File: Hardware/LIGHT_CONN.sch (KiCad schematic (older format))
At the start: 73 parts, among them P10 AI_RGB, P11 AI_RGB, P12 AI_RGB, P13 AI_RGB, P14 CONN_01X04, P15 AI_RGB, P16 AI_RGB, P17 AI_RGB, P18 AI_RGB, P19 AI_RGB, P2 AI_RGB, P20 CONN_01X04, P21 AI_RGB, P3 CONN_01X04, P4 AI_RGB, P5 AI_RGB, P6 AI_RGB, P7 AI_RGB, P8 AI_RGB, P9 CONN_01X04, Q10 MOSFET_N, Q11 MOSFET_N, Q12 MOSFET_N, Q13 MOSFET_N, Q2 MOSFET_N, Q3 MOSFET_N, Q4 MOSFET_N, Q5 MOSFET_N, Q6 MOSFET_N, Q7 MOSFET_N, Q8 MOSFET_N, Q9 MOSFET_N, U10 PCA9685BS

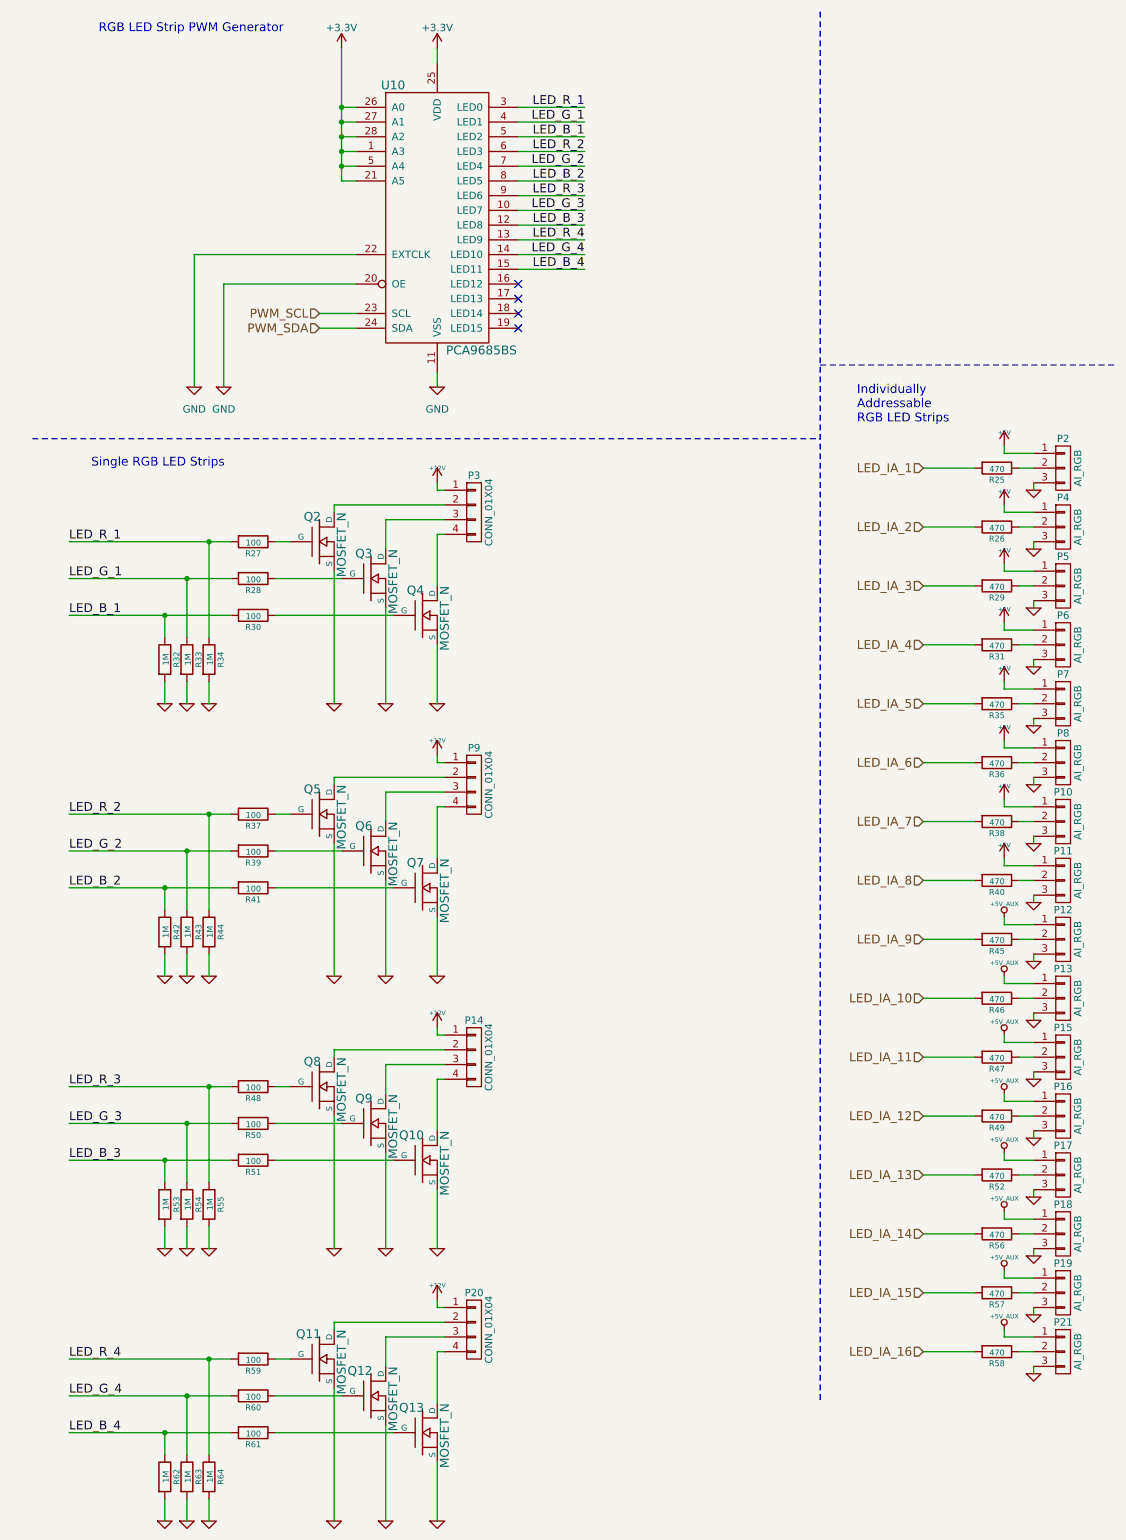
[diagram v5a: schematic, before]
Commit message: Finished converting to global labels
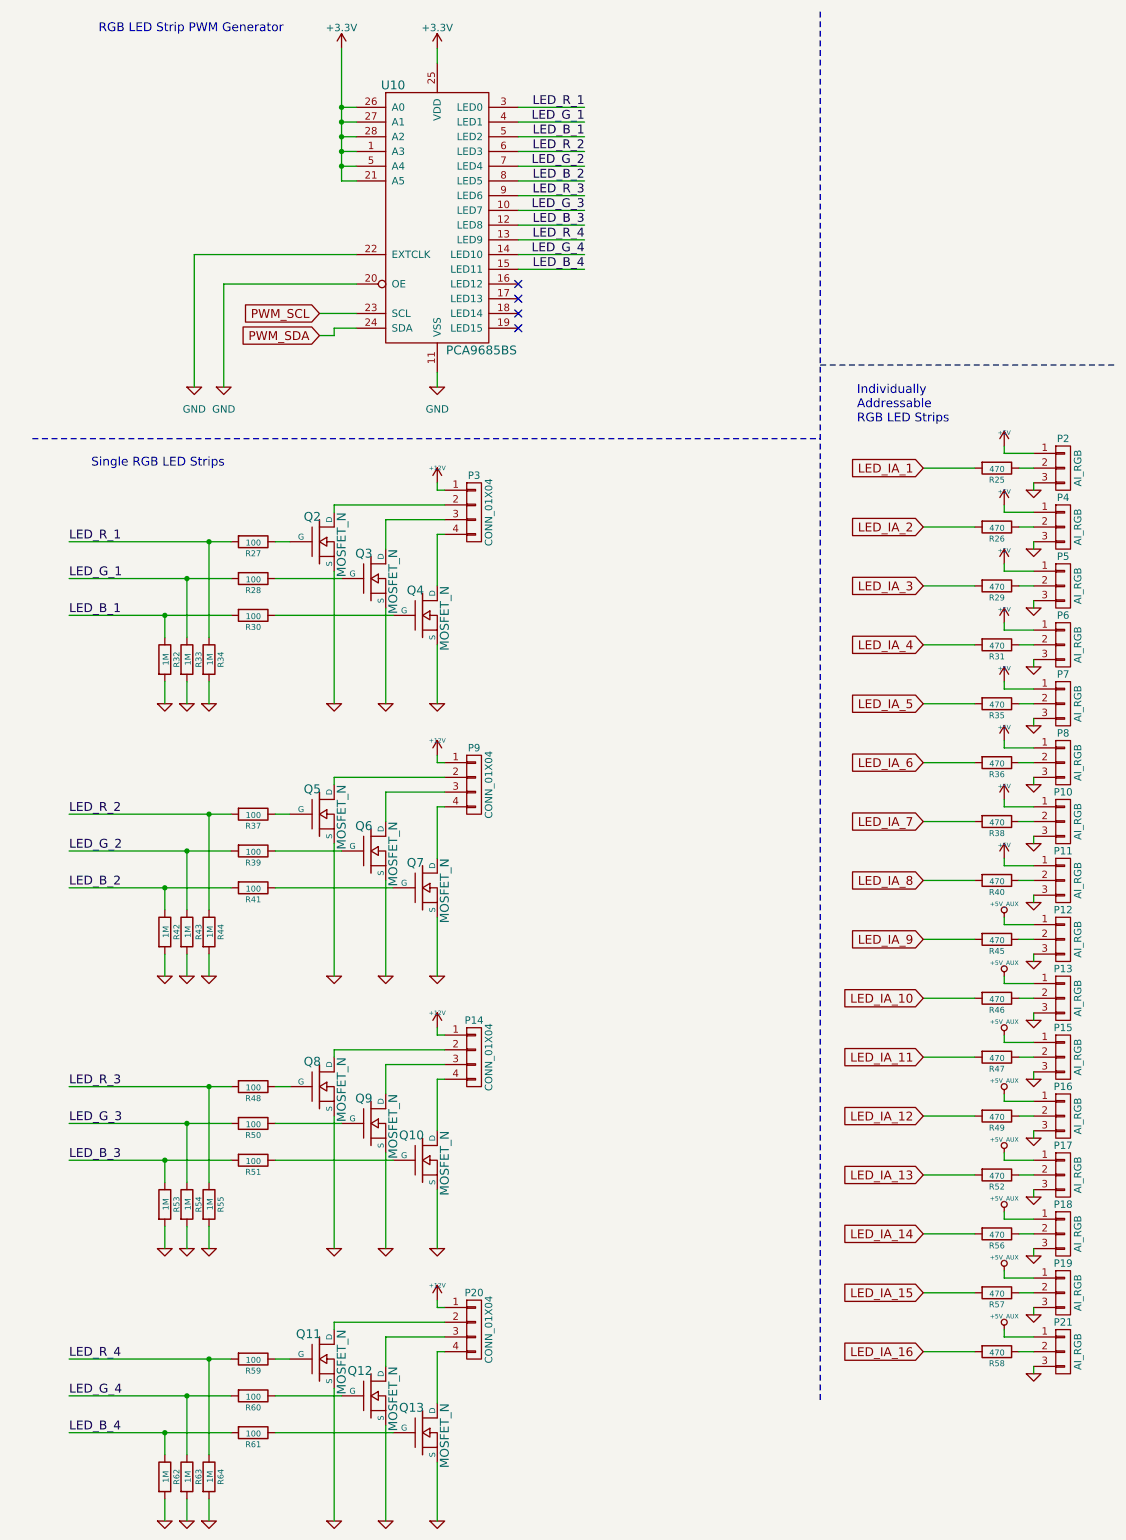
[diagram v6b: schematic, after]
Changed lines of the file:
@@
 $Descr A4 8268 11693 portrait
 encoding utf-8
-Sheet 5 8
+Sheet 10 10
 Title ""
 Date ""
@@
 	1    0    0    -1
 $EndComp
-Text HLabel 6500 3600 0    60   Input ~ 0
-LED_IA_1
-Text HLabel 6500 4000 0    60   Input ~ 0
-LED_IA_2
-Text HLabel 6500 4400 0    60   Input ~ 0
-LED_IA_3
-Text HLabel 6500 4800 0    60   Input ~ 0
-LED_IA_4
-Text HLabel 6500 5200 0    60   Input ~ 0
-LED_IA_5
-Text HLabel 6500 5600 0    60   Input ~ 0
-LED_IA_6
-Text HLabel 6500 6000 0    60   Input ~ 0
-LED_IA_7
-Text HLabel 6500 6400 0    60   Input ~ 0
-LED_IA_8
-Text HLabel 6500 6800 0    60   Input ~ 0
-LED_IA_9
-Text HLabel 6500 7200 0    60   Input ~ 0
-LED_IA_10
-Text HLabel 6500 7600 0    60   Input ~ 0
-LED_IA_11
-Text HLabel 6500 8000 0    60   Input ~ 0
-LED_IA_12
-Text HLabel 6500 8400 0    60   Input ~ 0
-LED_IA_13
-Text HLabel 6500 8800 0    60   Input ~ 0
-LED_IA_14
-Text HLabel 6500 9200 0    60   Input ~ 0
-LED_IA_15
-Text HLabel 6500 9600 0    60   Input ~ 0
-LED_IA_16
 $Comp
 L PCA9685BS U10
@@
 NoConn ~ 3750 2550
 NoConn ~ 3750 2650
-Text HLabel 2400 2550 0    60   Input ~ 0
-PWM_SCL
-Text HLabel 2400 2650 0    60   Input ~ 0
-PWM_SDA
 $Comp
 L GND-RESCUE-museV2 #PWR67
@@
 	1550 2150 2650 2150
 Wire Wire Line
-	2400 2650 2650 2650
-Wire Wire Line
 	2400 2550 2650 2550
 Wire Wire Line
@@
 Wire Notes Line
 	450  3400 5800 3400
-Wire Notes Line
-	5800 500  5800 9950
 Wire Wire Line
 	2500 9400 3250 9400
@@
 Wire Wire Line
 	7250 9600 7150 9600
+Text GLabel 2400 2550 0    60   Input ~ 0
+PWM_SCL
+Text GLabel 2400 2700 0    60   Input ~ 0
+PWM_SDA
+Wire Wire Line
+	2400 2700 2500 2700
+Wire Wire Line
+	2500 2700 2500 2650
+Wire Wire Line
+	2500 2650 2650 2650
+Text GLabel 6500 3600 0    60   Input ~ 0
+LED_IA_1
+Wire Notes Line
+	5800 500  5800 9950
+Text GLabel 6500 4000 0    60   Input ~ 0
+LED_IA_2
+Text GLabel 6500 4400 0    60   Input ~ 0
+LED_IA_3
+Text GLabel 6500 4800 0    60   Input ~ 0
+LED_IA_4
+Text GLabel 6500 5200 0    60   Input ~ 0
+LED_IA_5
+Text GLabel 6500 5600 0    60   Input ~ 0
+LED_IA_6
+Text GLabel 6500 6000 0    60   Input ~ 0
+LED_IA_7
+Text GLabel 6500 6400 0    60   Input ~ 0
+LED_IA_8
+Text GLabel 6500 6800 0    60   Input ~ 0
+LED_IA_9
+Text GLabel 6500 7200 0    60   Input ~ 0
+LED_IA_10
+Text GLabel 6500 7600 0    60   Input ~ 0
+LED_IA_11
+Text GLabel 6500 8000 0    60   Input ~ 0
+LED_IA_12
+Text GLabel 6500 8400 0    60   Input ~ 0
+LED_IA_13
+Text GLabel 6500 8800 0    60   Input ~ 0
+LED_IA_14
+Text GLabel 6500 9200 0    60   Input ~ 0
+LED_IA_15
+Text GLabel 6500 9600 0    60   Input ~ 0
+LED_IA_16
 $EndSCHEMATC

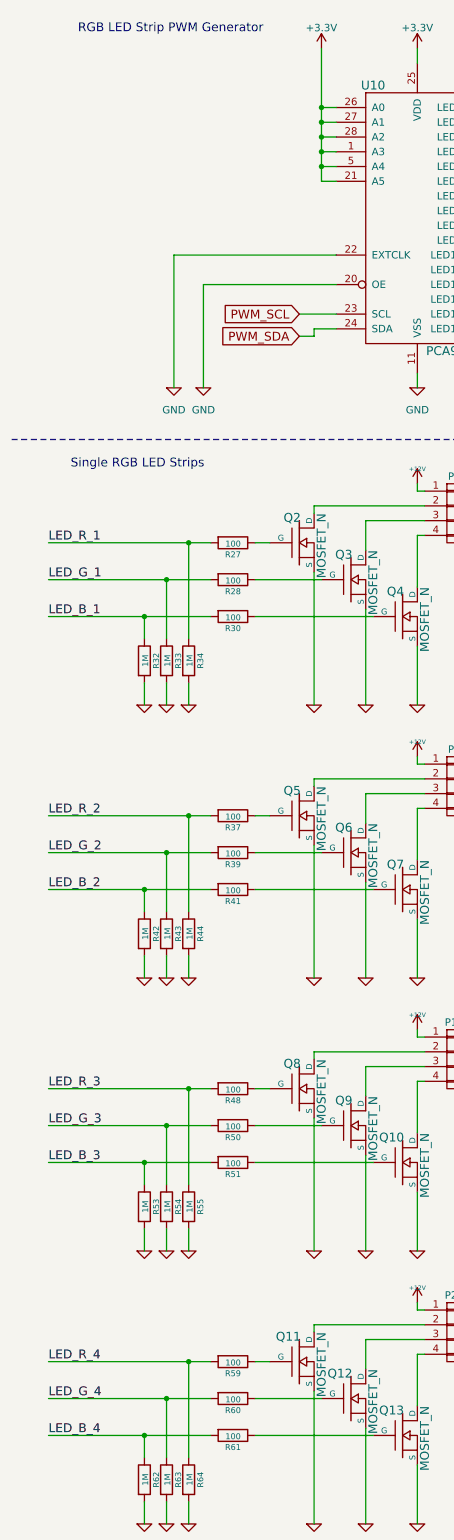
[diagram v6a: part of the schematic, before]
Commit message: Updated I2C pullup resistors and labels
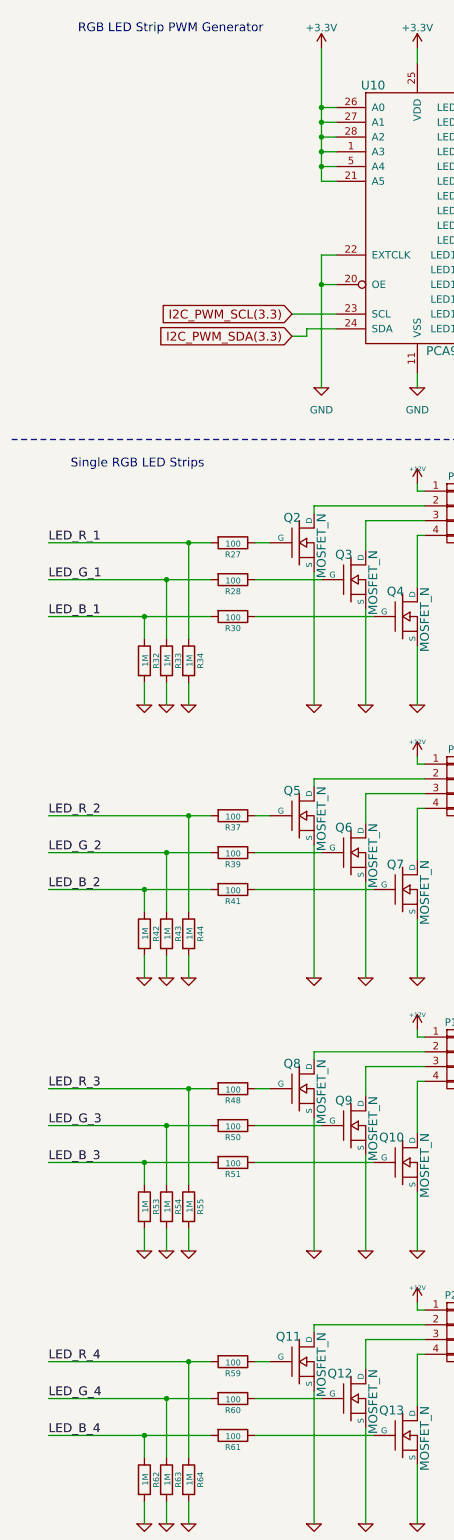
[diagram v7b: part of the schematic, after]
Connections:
- net PWM_SCL renamed I2C_PWM_SCL(3.3)
- net PWM_SDA renamed I2C_PWM_SDA(3.3)
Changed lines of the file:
@@
 NoConn ~ 3750 2550
 NoConn ~ 3750 2650
-$Comp
-L GND-RESCUE-museV2 #PWR67
-U 1 1 57E689F1
-P 1550 3050
-F 0 "#PWR67" H 1550 2800 50  0001 C CNN
-F 1 "GND" H 1550 2900 50  0000 C CNN
-F 2 "" H 1550 3050 50  0000 C CNN
-F 3 "" H 1550 3050 50  0000 C CNN
-	1    1550 3050
-	1    0    0    -1
-$EndComp
-Wire Wire Line
-	1550 3050 1550 2150
-Wire Wire Line
-	1550 2150 2650 2150
-Wire Wire Line
-	2400 2550 2650 2550
+Wire Wire Line
+	2350 2550 2650 2550
 Wire Wire Line
 	3750 2250 4200 2250
@@
 	6500 9600 6850 9600
 Wire Wire Line
-	700  4600 1800 4600
-Wire Wire Line
-	700  4350 1800 4350
-Wire Wire Line
-	700  4100 1800 4100
+	700  4600 1350 4600
+Wire Wire Line
+	1350 4600 1800 4600
+Wire Wire Line
+	700  4350 1500 4350
+Wire Wire Line
+	1500 4350 1800 4350
+Wire Wire Line
+	700  4100 1650 4100
+Wire Wire Line
+	1650 4100 1800 4100
 Wire Wire Line
 	2100 4350 2550 4350
@@
 	3200 7050 3200 6650
 Wire Wire Line
-	700  6450 1800 6450
-Wire Wire Line
-	700  6200 1800 6200
-Wire Wire Line
-	700  5950 1800 5950
+	700  6450 1350 6450
+Wire Wire Line
+	1350 6450 1800 6450
+Wire Wire Line
+	700  6200 1500 6200
+Wire Wire Line
+	1500 6200 1800 6200
+Wire Wire Line
+	700  5950 1650 5950
+Wire Wire Line
+	1650 5950 1800 5950
 Wire Wire Line
 	2100 6200 2550 6200
@@
 	3200 8900 3200 8500
 Wire Wire Line
-	700  8300 1800 8300
-Wire Wire Line
-	700  8050 1800 8050
-Wire Wire Line
-	700  7800 1800 7800
+	700  8300 1350 8300
+Wire Wire Line
+	1350 8300 1800 8300
+Wire Wire Line
+	700  8050 1500 8050
+Wire Wire Line
+	1500 8050 1800 8050
+Wire Wire Line
+	700  7800 1650 7800
+Wire Wire Line
+	1650 7800 1800 7800
 Wire Wire Line
 	2100 8050 2550 8050
@@
 	3200 10750 3200 10350
 Wire Wire Line
-	700  10150 1800 10150
-Wire Wire Line
-	700  9900 1800 9900
-Wire Wire Line
-	700  9650 1800 9650
+	700  10150 1350 10150
+Wire Wire Line
+	1350 10150 1800 10150
+Wire Wire Line
+	700  9900 1500 9900
+Wire Wire Line
+	1500 9900 1800 9900
+Wire Wire Line
+	700  9650 1650 9650
+Wire Wire Line
+	1650 9650 1800 9650
 Wire Wire Line
 	2100 9900 2550 9900
@@
 $EndComp
 Wire Wire Line
-	2550 750  2550 1650
+	2550 750  2550 1150
+Wire Wire Line
+	2550 1150 2550 1250
+Wire Wire Line
+	2550 1250 2550 1350
+Wire Wire Line
+	2550 1350 2550 1450
+Wire Wire Line
+	2550 1450 2550 1550
+Wire Wire Line
+	2550 1550 2550 1650
 Wire Wire Line
 	2550 1650 2650 1650
@@
 L GND-RESCUE-museV2 #PWR68
 U 1 1 57EF1660
-P 1750 3050
-F 0 "#PWR68" H 1750 2800 50  0001 C CNN
-F 1 "GND" H 1750 2900 50  0000 C CNN
-F 2 "" H 1750 3050 50  0000 C CNN
-F 3 "" H 1750 3050 50  0000 C CNN
-	1    1750 3050
+P 2550 3050
+F 0 "#PWR68" H 2550 2800 50  0001 C CNN
+F 1 "GND" H 2550 2900 50  0000 C CNN
+F 2 "" H 2550 3050 50  0000 C CNN
+F 3 "" H 2550 3050 50  0000 C CNN
+	1    2550 3050
 	1    0    0    -1
 $EndComp
 Wire Wire Line
-	1750 2350 1750 3050
-Wire Wire Line
-	1750 2350 2650 2350
+	2550 2150 2550 2350
+Wire Wire Line
+	2550 2350 2550 3050
+Wire Wire Line
+	2550 2350 2650 2350
 Wire Wire Line
 	2200 9650 2100 9650
@@
 Wire Wire Line
 	7250 9600 7150 9600
-Text GLabel 2400 2550 0    60   Input ~ 0
-PWM_SCL
-Text GLabel 2400 2700 0    60   Input ~ 0
-PWM_SDA
-Wire Wire Line
-	2400 2700 2500 2700
-Wire Wire Line
-	2500 2700 2500 2650
-Wire Wire Line
-	2500 2650 2650 2650
+Text GLabel 2350 2550 0    60   Input ~ 0
+I2C_PWM_SCL(3.3)
+Text GLabel 2350 2700 0    60   Input ~ 0
+I2C_PWM_SDA(3.3)
+Wire Wire Line
+	2350 2700 2450 2700
+Wire Wire Line
+	2450 2700 2450 2650
+Wire Wire Line
+	2450 2650 2650 2650
 Text GLabel 6500 3600 0    60   Input ~ 0
 LED_IA_1
@@
 Text GLabel 6500 9600 0    60   Input ~ 0
 LED_IA_16
+Wire Wire Line
+	2650 2150 2550 2150
+Connection ~ 2550 2350
 $EndSCHEMATC
